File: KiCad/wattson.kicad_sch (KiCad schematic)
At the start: 28 parts, among them Q1 NPN, Q2 NPN, SW1 Keypad 1, SW10 Plug, SW11 On/Off, SW2 Keypad 2, SW3 Keypad 3, SW4 Keypad 4, SW5 Keypad 5, SW6 Keypad 0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

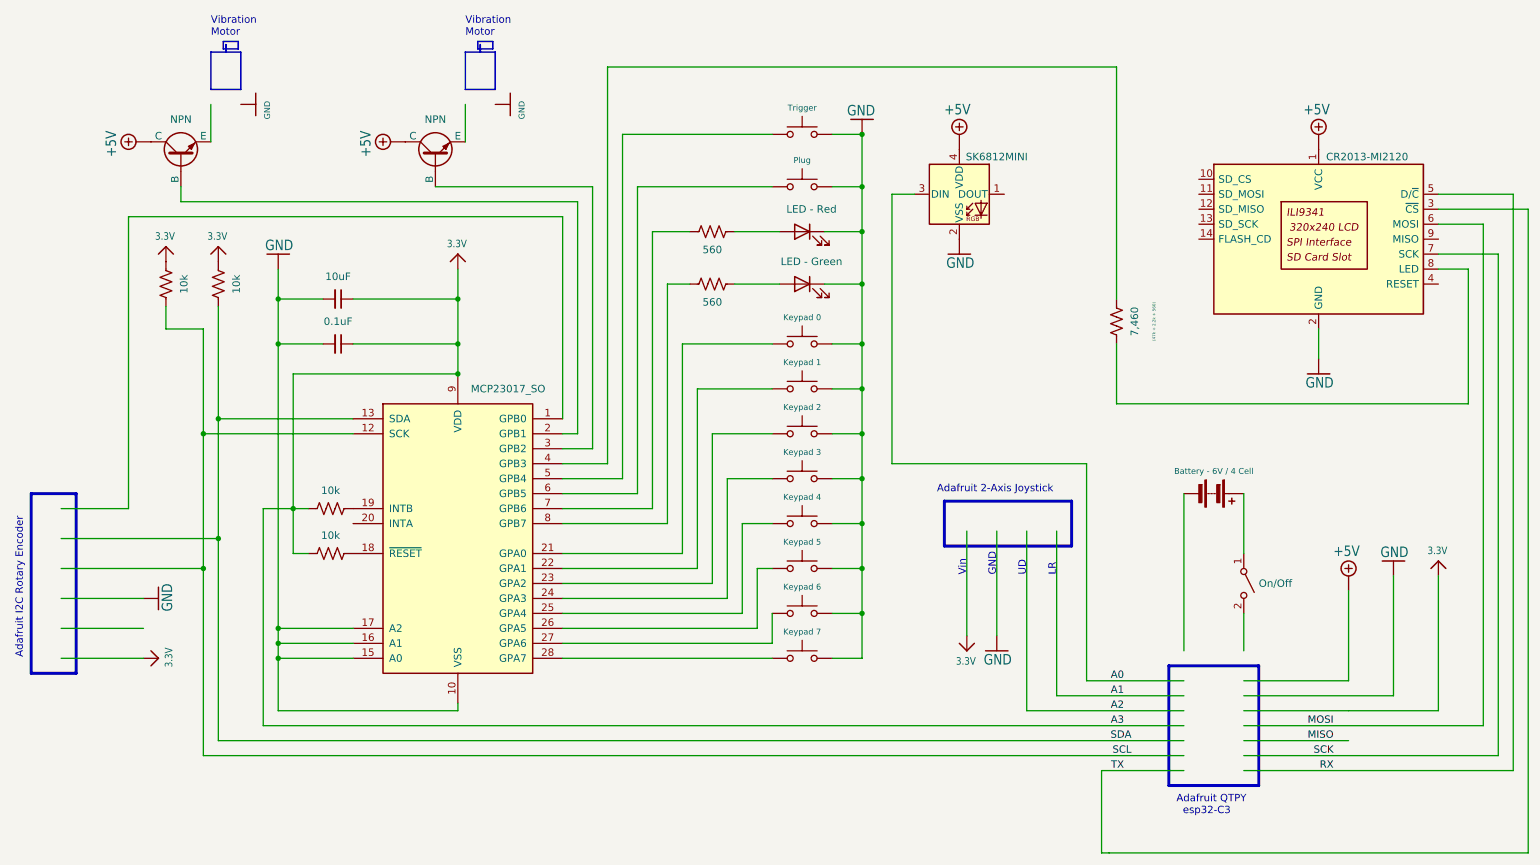
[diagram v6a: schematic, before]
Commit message: switch to ESP32-S2
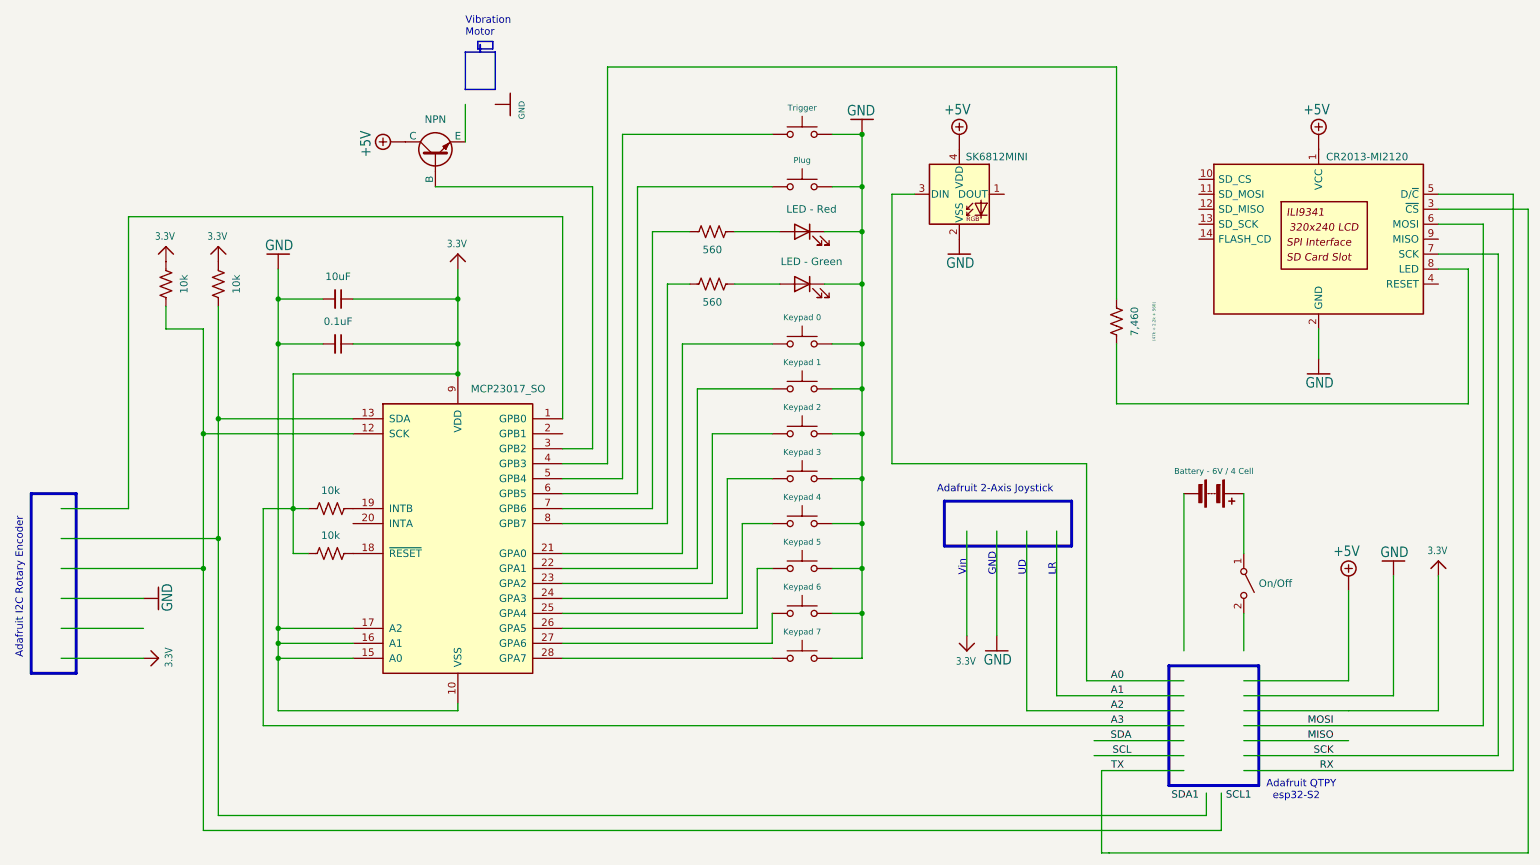
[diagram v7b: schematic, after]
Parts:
- removed Q1: NPN, symbol Simulation_SPICE:NPN
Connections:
- net SCL: no longer R2.2, U2.12 (SCK)
- net SDA: no longer R1.2, U2.13 (SDA)
- new net: R1.2, U2.13 (SDA)
- new net: R2.2, U2.12 (SCK)
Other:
- note added: "Adafruit QTPY esp32-S2"
- note removed: "Adafruit QTPY esp32-C3"
